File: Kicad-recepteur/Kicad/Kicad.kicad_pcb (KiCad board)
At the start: 4 copper layers, 32.1 x 30 mm, 27 parts, among them J1 Conn_02x07_Odd_Even, J3 Conn_01x04, J4 Conn_01x02, J42 Conn_01x04, J5 USB_C_Receptacle_PowerOnly_6P, U1 STM32L021K4Tx, U2 BU33SD5WG-TR

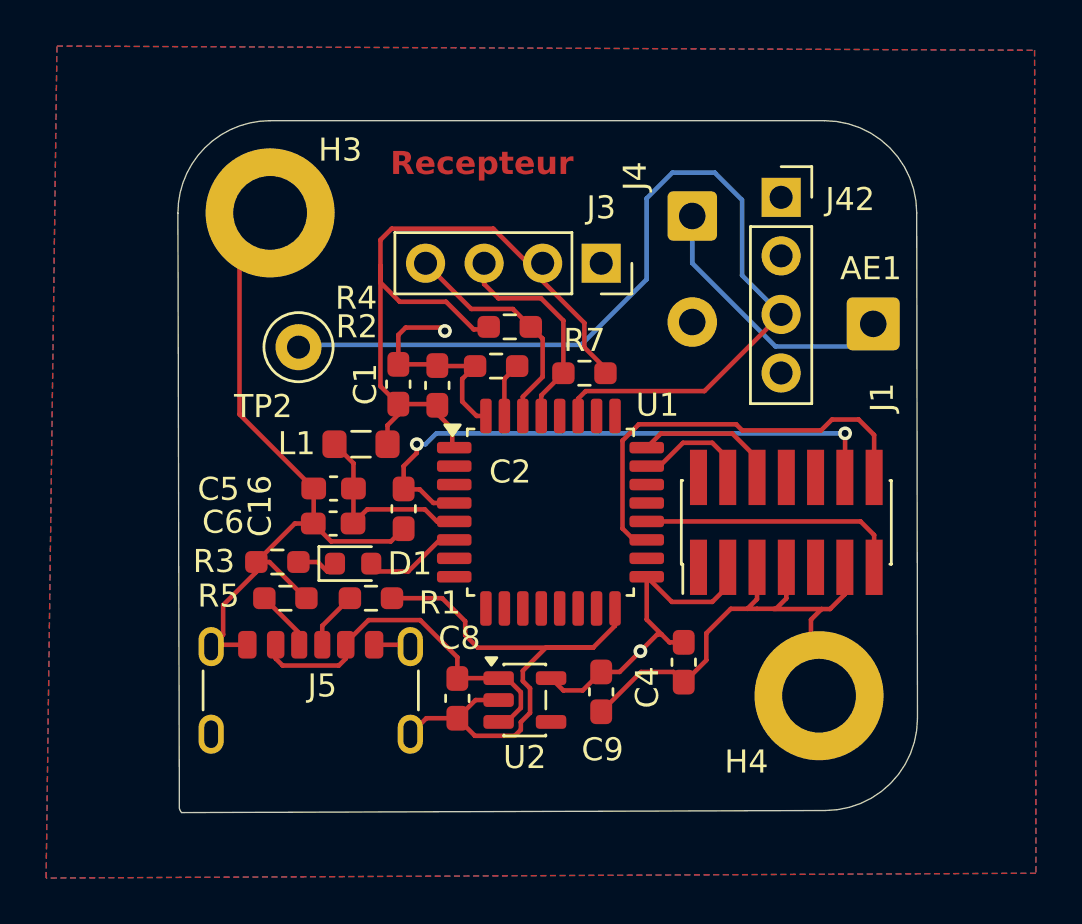
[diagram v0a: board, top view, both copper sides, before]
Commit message: feat: Add initial KiCad PCB layout for the receiver module.
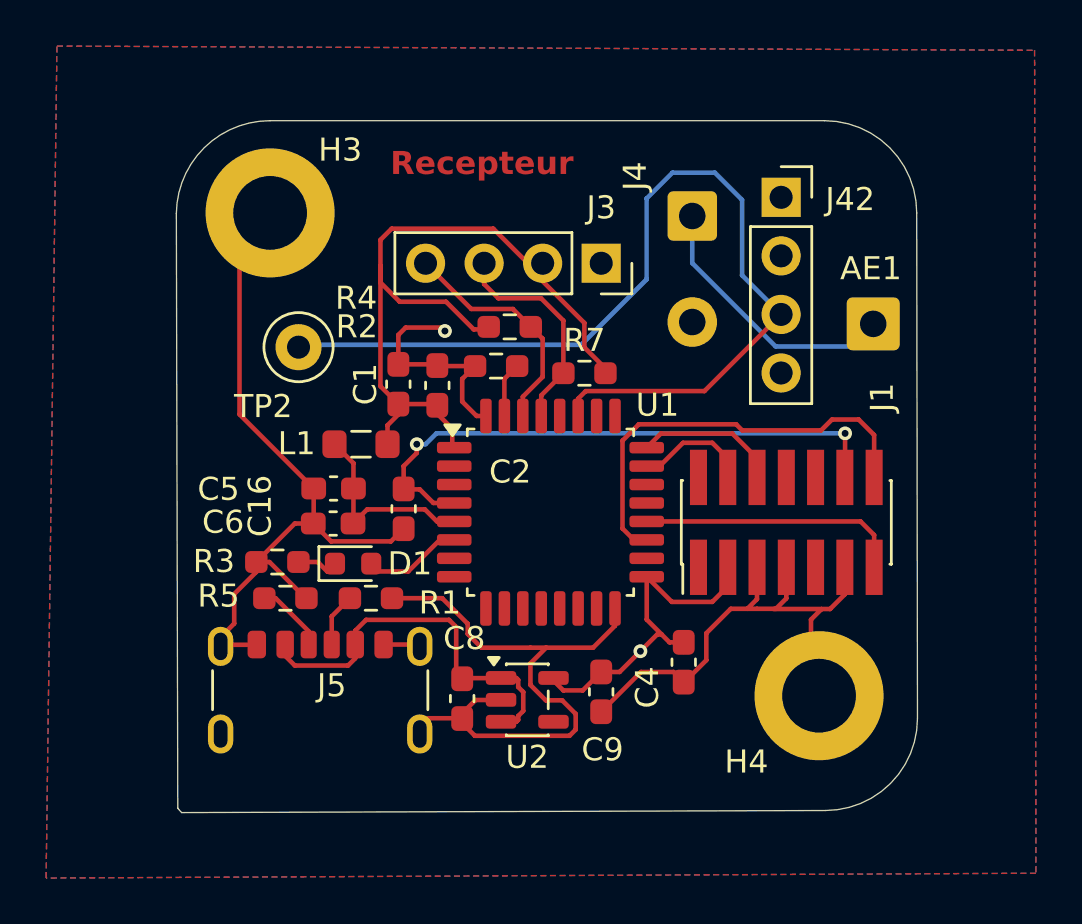
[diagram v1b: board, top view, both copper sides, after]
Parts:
- moved J5 0.41 mm to (101.6, 115.1)
- moved C8 0.21 mm to (107.7, 114.4)
- moved U2 0.11 mm to (110.6, 114.4)
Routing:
- net +5V: track 16.3 -> 18.1 mm
- net GND: track 95.0 -> 95.5 mm
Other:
- board size 32.1 x 30 mm -> 32.2 x 30 mm
